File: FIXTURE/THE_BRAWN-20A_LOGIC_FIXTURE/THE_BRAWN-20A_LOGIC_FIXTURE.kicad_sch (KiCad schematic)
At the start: 54 parts, among them J1 Pins_2.54_1x3, J2 Pins_2.54_1x3, J5 Pins_2.54_1x2, M1 Mount_M3, M10 Mount_M3, M11 Mount_M3, M12 Mount_M3, M13 Mount_M3, M14 Mount_M3, M2 Mount_M3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

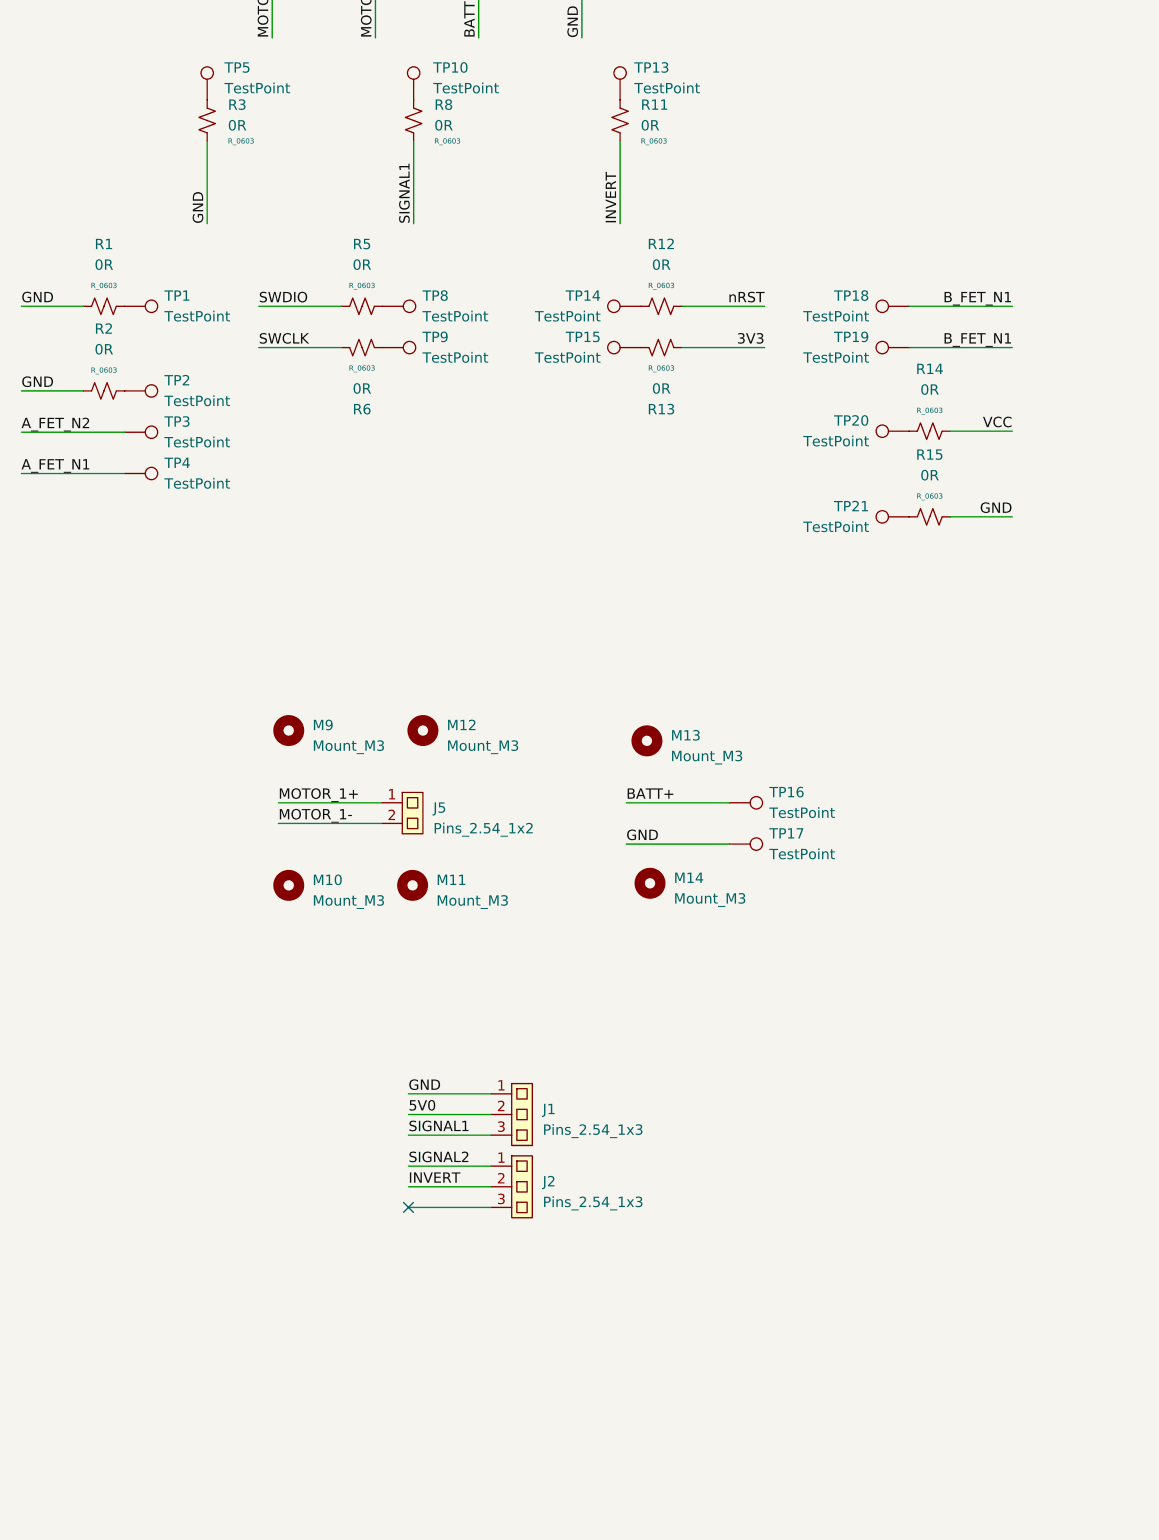
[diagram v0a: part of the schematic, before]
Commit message: Finish Tracking Logic Fixture PCB
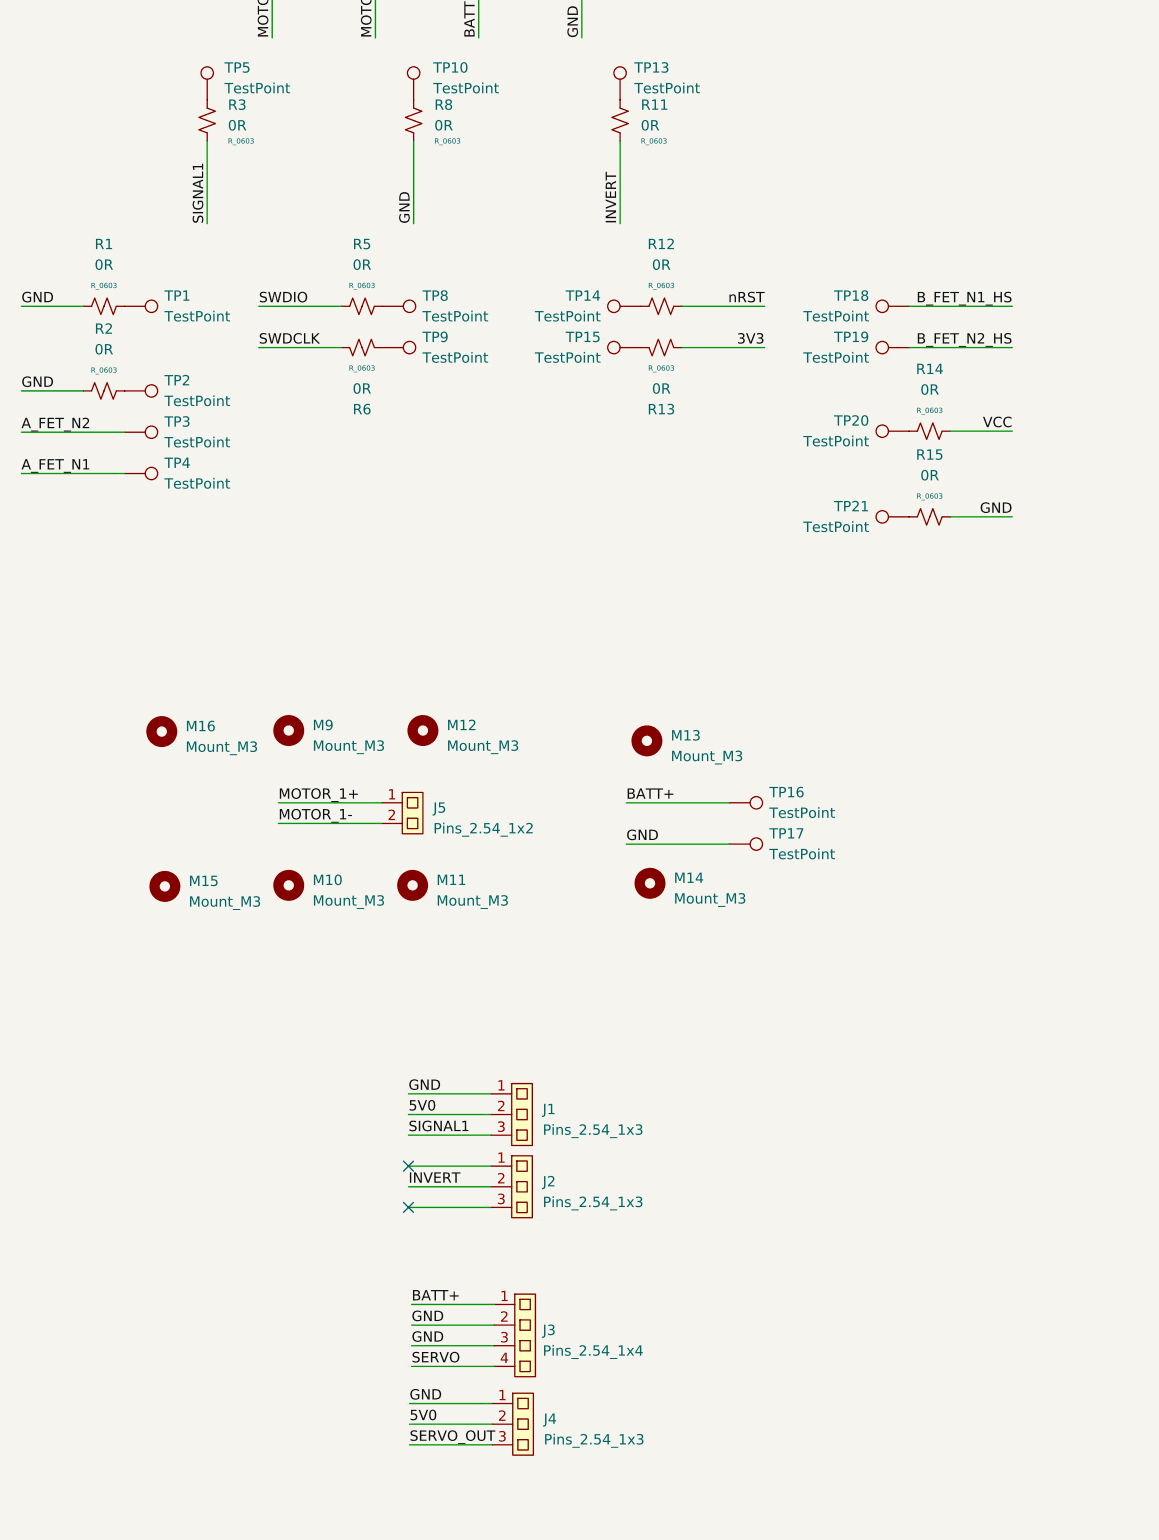
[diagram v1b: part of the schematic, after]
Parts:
- added J3: Pins_2.54_1x4, J_Connector:Pins-2.54-1x4, symbol .J_Connector:Pins_2.54_1x4
- added J4: Pins_2.54_1x3, .J_Connector:Pins-2.54-1x3, symbol .J_Connector:Pins_2.54_1x3
- added M15, M16: Mount_M3, .M_Mechanical:Mount_M3, symbol .M_Mechanical:Mount_M3
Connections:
- net SWCLK is gone; now on net SWDCLK: R6.1
- net 5V0: now also J4.2
- net BATT+: now also J3.1
- net GND: now also R8.2, J3.2, J3.3, J4.1; no longer R3.2
- net SIGNAL1: now also R3.2; no longer R8.2
- net B_FET_N1 renamed B_FET_N1_HS
- net B_FET_N1_HS: no longer TP19.1
- net SIGNAL2: no longer names the net of J2.1
- new net B_FET_N2_HS: TP19.1
- new net SERVO: J3.4
- new net SERVO_OUT: J4.3
- no-connect marks 6 -> 7
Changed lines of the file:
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@@
     (company "CB-TECHNOLOGY")
   )
+  (no_connect (at 208.28 193.04))
   (no_connect (at 90.678 205.105))
   (no_connect (at 108.458 200.025))
@@
     (stroke (width 0) (type default))
   )
+  (wire (pts (xy 208.915 66.929) (xy 208.915 77.089))
+    (stroke (width 0) (type default))
+  )
   (wire (pts (xy 234.315 66.929) (xy 234.315 77.089))
     (stroke (width 0) (type default))
@@
     (stroke (width 0) (type default))
   )
+  (wire (pts (xy 183.515 66.929) (xy 183.515 77.089))
+    (stroke (width 0) (type default))
+  )
   (wire (pts (xy 168.275 97.663) (xy 160.655 97.663))
     (stroke (width 0) (type default))
@@
     (stroke (width 0) (type default))
   )
+  (wire (pts (xy 218.567 224.79) (xy 208.407 224.79))
+    (stroke (width 0) (type default))
+  )
   (wire (pts (xy 274.955 113.157) (xy 282.575 113.157))
     (stroke (width 0) (type default))
   )
+  (wire (pts (xy 218.821 212.598) (xy 208.661 212.598))
+    (stroke (width 0) (type default))
+  )
   (wire (pts (xy 204.978 150.876) (xy 192.278 150.876))
     (stroke (width 0) (type default))
@@
     (stroke (width 0) (type default))
   )
-  (wire (pts (xy 183.515 66.929) (xy 183.515 77.089))
+  (wire (pts (xy 218.567 222.25) (xy 208.407 222.25))
+    (stroke (width 0) (type default))
+  )
+  (wire (pts (xy 218.821 210.058) (xy 208.661 210.058))
     (stroke (width 0) (type default))
   )
@@
     (stroke (width 0) (type default))
   )
-  (wire (pts (xy 208.915 66.929) (xy 208.915 77.089))
+  (wire (pts (xy 218.821 217.678) (xy 208.661 217.678))
+    (stroke (width 0) (type default))
+  )
+  (wire (pts (xy 218.821 215.138) (xy 208.661 215.138))
+    (stroke (width 0) (type default))
+  )
+  (wire (pts (xy 218.567 227.33) (xy 208.407 227.33))
     (stroke (width 0) (type default))
   )
@@
     (effects (font (size 1.27 1.27)) (justify left bottom))
   )
+  (label "GND" (at 208.661 212.598 0) (fields_autoplaced)
+    (effects (font (size 1.27 1.27)) (justify left bottom))
+  )
+  (label "GND" (at 208.661 215.138 0) (fields_autoplaced)
+    (effects (font (size 1.27 1.27)) (justify left bottom))
+  )
   (label "BATT+" (at 235.077 148.336 0) (fields_autoplaced)
     (effects (font (size 1.27 1.27)) (justify left bottom))
@@
     (effects (font (size 1.27 1.27)) (justify left bottom))
   )
-  (label "SWCLK" (at 189.865 92.329 0) (fields_autoplaced)
+  (label "SWDCLK" (at 189.865 92.329 0) (fields_autoplaced)
     (effects (font (size 1.27 1.27)) (justify left bottom))
   )
@@
     (effects (font (size 1.27 1.27)) (justify left bottom))
   )
+  (label "GND" (at 208.915 77.089 90) (fields_autoplaced)
+    (effects (font (size 1.27 1.27)) (justify left bottom))
+  )
   (label "GND" (at 229.616 54.229 90) (fields_autoplaced)
     (effects (font (size 1.27 1.27)) (justify left bottom))
@@
     (effects (font (size 1.27 1.27)) (justify left bottom))
   )
+  (label "5V0" (at 208.407 224.79 0) (fields_autoplaced)
+    (effects (font (size 1.27 1.27)) (justify left bottom))
+  )
+  (label "BATT+" (at 208.661 210.058 0) (fields_autoplaced)
+    (effects (font (size 1.27 1.27)) (justify left bottom))
+  )
   (label "A_FET_N2" (at 160.655 102.743 0) (fields_autoplaced)
     (effects (font (size 1.27 1.27)) (justify left bottom))
@@
   )
   (label "MOTOR_1+" (at 191.516 54.229 90) (fields_autoplaced)
+    (effects (font (size 1.27 1.27)) (justify left bottom))
+  )
+  (label "SIGNAL1" (at 183.515 77.089 90) (fields_autoplaced)
     (effects (font (size 1.27 1.27)) (justify left bottom))
   )
@@
     (effects (font (size 1.27 1.27)) (justify right bottom))
   )
+  (label "GND" (at 208.407 222.25 0) (fields_autoplaced)
+    (effects (font (size 1.27 1.27)) (justify left bottom))
+  )
   (label "SWDCLK" (at 77.978 202.565 0) (fields_autoplaced)
     (effects (font (size 1.27 1.27)) (justify left bottom))
@@
     (effects (font (size 1.27 1.27)) (justify left bottom))
   )
-  (label "B_FET_N1" (at 282.575 87.249 180) (fields_autoplaced)
+  (label "B_FET_N1_HS" (at 282.575 87.249 180) (fields_autoplaced)
     (effects (font (size 1.27 1.27)) (justify right bottom))
   )
@@
     (effects (font (size 1.27 1.27)) (justify right bottom))
   )
-  (label "GND" (at 183.515 77.089 90) (fields_autoplaced)
-    (effects (font (size 1.27 1.27)) (justify left bottom))
-  )
-  (label "SIGNAL1" (at 208.915 77.089 90) (fields_autoplaced)
-    (effects (font (size 1.27 1.27)) (justify left bottom))
-  )
-  (label "SIGNAL2" (at 208.28 193.04 0) (fields_autoplaced)
-    (effects (font (size 1.27 1.27)) (justify left bottom))
-  )
-  (label "B_FET_N1" (at 282.575 92.329 180) (fields_autoplaced)
+  (label "B_FET_N2_HS" (at 282.575 92.329 180) (fields_autoplaced)
     (effects (font (size 1.27 1.27)) (justify right bottom))
   )
@@
   )
   (label "GND" (at 235.077 153.416 0) (fields_autoplaced)
+    (effects (font (size 1.27 1.27)) (justify left bottom))
+  )
+  (label "SERVO_OUT" (at 208.407 227.33 0) (fields_autoplaced)
+    (effects (font (size 1.27 1.27)) (justify left bottom))
+  )
+  (label "SERVO" (at 208.661 217.678 0) (fields_autoplaced)
     (effects (font (size 1.27 1.27)) (justify left bottom))
   )
@@
         (path "/e63e39d7-6ac0-4ffd-8aa3-1841a4541b55"
           (reference "TP7") (unit 1)
+        )
+      )
+    )
+  )
+  (symbol (lib_id ".J_Connector:Pins_2.54_1x3") (at 222.377 228.6 0) (unit 1)
+    (in_bom yes) (on_board yes) (dnp no) (fields_autoplaced)
+    (property "Reference" "J4" (at 224.917 224.155 0)
+      (effects (font (size 1.27 1.27)) (justify left))
+    )
+    (property "Value" "Pins_2.54_1x3" (at 224.917 226.695 0)
+      (effects (font (size 1.27 1.27)) (justify left))
+    )
+    (property "Footprint" ".J_Connector:Pins-2.54-1x3" (at 222.377 231.775 0)
+      (effects (font (size 1.27 1.27)) hide)
+    )
+    (property "Datasheet" "" (at 222.377 228.6 0)
+      (effects (font (size 1.27 1.27)) hide)
+    )
+    (pin "1")
+    (pin "2")
+    (pin "3")
+    (instances
+      (project "THE_BRAWN-20A_LOGIC_FIXTURE"
+        (path "/e63e39d7-6ac0-4ffd-8aa3-1841a4541b55"
+          (reference "J4") (unit 1)
         )
       )
@@
     )
   )
+  (symbol (lib_id ".M_Mechanical:Mount_M3") (at 178.308 158.623 0) (unit 1)
+    (in_bom no) (on_board yes) (dnp no) (fields_autoplaced)
+    (property "Reference" "M15" (at 181.229 157.988 0)
+      (effects (font (size 1.27 1.27)) (justify left))
+    )
+    (property "Value" "Mount_M3" (at 181.229 160.528 0)
+      (effects (font (size 1.27 1.27)) (justify left))
+    )
+    (property "Footprint" ".M_Mechanical:Mount_M3" (at 178.308 164.973 0)
+      (effects (font (size 1.27 1.27)) hide)
+    )
+    (property "Datasheet" "" (at 157.988 163.703 0)
+      (effects (font (size 1.27 1.27)) hide)
+    )
+    (instances
+      (project "THE_BRAWN-20A_LOGIC_FIXTURE"
+        (path "/e63e39d7-6ac0-4ffd-8aa3-1841a4541b55"
+          (reference "M15") (unit 1)
+        )
+      )
+    )
+  )
   (symbol (lib_id ".M_Mechanical:Mount_M3") (at 372.1862 233.4006 0) (unit 1)
     (in_bom no) (on_board yes) (dnp no) (fields_autoplaced)
@@
     )
   )
+  (symbol (lib_id ".J_Connector:Pins_2.54_1x4") (at 222.631 218.948 0) (unit 1)
+    (in_bom yes) (on_board yes) (dnp no) (fields_autoplaced)
+    (property "Reference" "J3" (at 224.79 213.233 0)
+      (effects (font (size 1.27 1.27)) (justify left))
+    )
+    (property "Value" "Pins_2.54_1x4" (at 224.79 215.773 0)
+      (effects (font (size 1.27 1.27)) (justify left))
+    )
+    (property "Footprint" "J_Connector:Pins-2.54-1x4" (at 222.631 222.123 0)
+      (effects (font (size 1.27 1.27)) hide)
+    )
+    (property "Datasheet" "" (at 222.631 218.948 0)
+      (effects (font (size 1.27 1.27)) hide)
+    )
+    (pin "1")
+    (pin "2")
+    (pin "3")
+    (pin "4")
+    (instances
+      (project "THE_BRAWN-20A_LOGIC_FIXTURE"
+        (path "/e63e39d7-6ac0-4ffd-8aa3-1841a4541b55"
+          (reference "J3") (unit 1)
+        )
+      )
+    )
+  )
   (symbol (lib_id ".R_Resistor:R_0603") (at 229.616 41.529 0) (unit 1)
     (in_bom yes) (on_board yes) (dnp no) (fields_autoplaced)
@@
         )
       )
+    )
+  )
+  (symbol (lib_id ".M_Mechanical:Mount_M3") (at 177.927 139.573 0) (unit 1)
+    (in_bom no) (on_board yes) (dnp no) (fields_autoplaced)
+    (property "Reference" "M16" (at 180.848 138.938 0)
+      (effects (font (size 1.27 1.27)) (justify left))
+    )
+    (property "Value" "Mount_M3" (at 180.848 141.478 0)
+      (effects (font (size 1.27 1.27)) (justify left))
+    )
+    (property "Footprint" ".M_Mechanical:Mount_M3" (at 177.927 145.923 0)
+      (effects (font (size 1.27 1.27)) hide)
+    )
+    (property "Datasheet" "" (at 157.607 144.653 0)
+      (effects (font (size 1.27 1.27)) hide)
+    )
+    (instances
+      (project "THE_BRAWN-20A_LOGIC_FIXTURE"
+        (path "/e63e39d7-6ac0-4ffd-8aa3-1841a4541b55"
+          (reference "M16") (unit 1)
+        )
+      )
